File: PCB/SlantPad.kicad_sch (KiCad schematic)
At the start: 33 parts, among them SW1 SW_Push, SW10 RotaryEncoder_Switch, SW2 SW_Push, SW3 SW_Push, SW4 SW_Push, SW5 SW_Push, SW6 SW_Push, SW7 SW_Push, SW8 SW_Push, SW9 SW_Push, U1 XIAO-RP2040-DIP

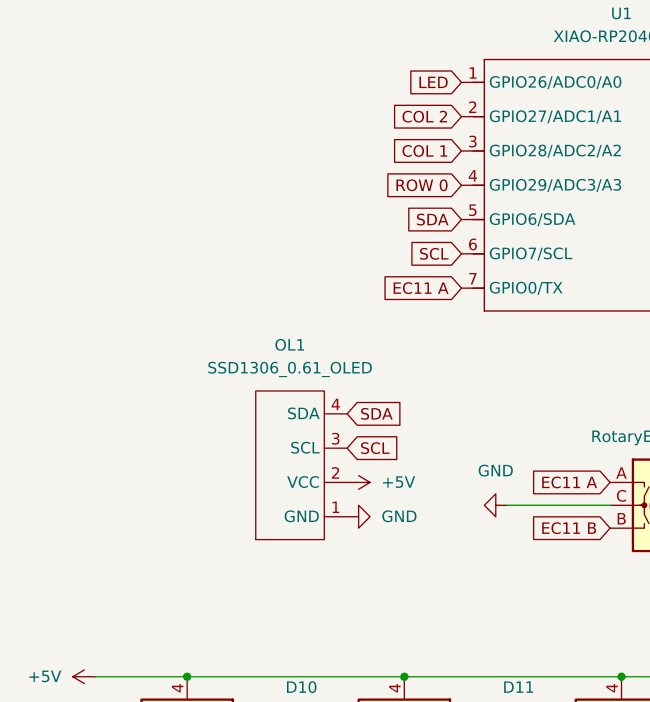
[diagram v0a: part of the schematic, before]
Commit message: no backlighting 😔 alr ordered pcb and apparently used wrong neopixel footprint
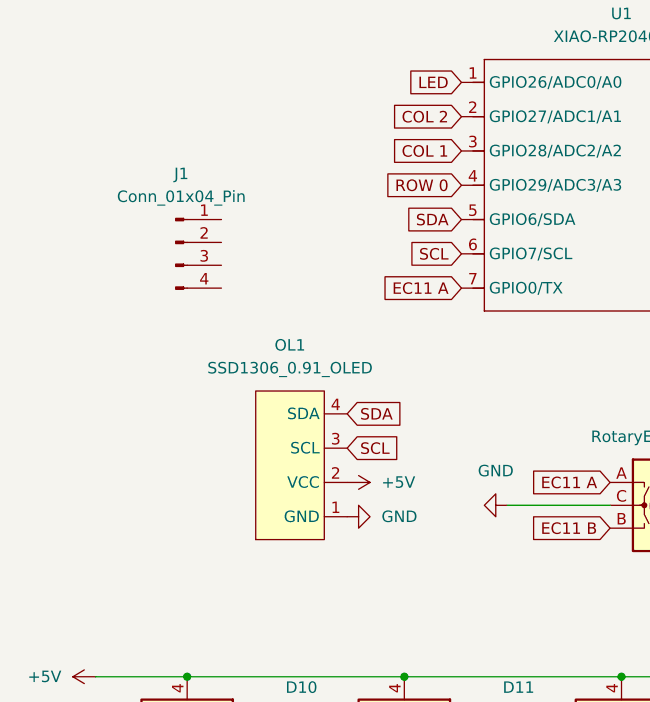
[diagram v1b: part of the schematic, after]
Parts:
- added J1: Conn_01x04_Pin, symbol Connector:Conn_01x04_Pin
- OL1: value SSD1306_0.61_OLED -> SSD1306_0.91_OLED
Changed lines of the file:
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@@
+	)
+	(symbol
+		(lib_id "Connector:Conn_01x04_Pin")
+		(at 46.99 50.8 0)
+		(unit 1)
+		(exclude_from_sim no)
+		(in_bom yes)
+		(on_board yes)
+		(dnp no)
+		(fields_autoplaced yes)
+		(property "Reference" "J1"
+			(at 47.625 43.18 0)
+			(effects
+				(font
+					(size 1.27 1.27)
+				)
+			)
+		)
+		(property "Value" "Conn_01x04_Pin"
+			(at 47.625 45.72 0)
+			(effects
+				(font
+					(size 1.27 1.27)
+				)
+			)
+		)
+		(property "Footprint" ""
+			(at 46.99 50.8 0)
+			(effects
+				(font
+					(size 1.27 1.27)
+				)
+				(hide yes)
+			)
+		)
+		(property "Datasheet" "~"
+			(at 46.99 50.8 0)
+			(effects
+				(font
+					(size 1.27 1.27)
+				)
+				(hide yes)
+			)
+		)
+		(property "Description" "Generic connector, single row, 01x04, script generated"
+			(at 46.99 50.8 0)
+			(effects
+				(font
+					(size 1.27 1.27)
+				)
+				(hide yes)
+			)
+		)
+		(pin "2"
+		)
+		(pin "1"
+		)
+		(pin "4"
+		)
+		(pin "3"
+		)
+		(instances
+			(project ""
+				(path "/35c226b8-067d-4b5d-985c-4ff5d6b31bfb"
+					(reference "J1")
+					(unit 1)
+				)
+			)
+		)
 	)
 	(symbol
@@
 			)
 		)
-		(property "Value" "SSD1306_0.61_OLED"
+		(property "Value" "SSD1306_0.91_OLED"
 			(at 59.69 64.77 90)
 			(effects
